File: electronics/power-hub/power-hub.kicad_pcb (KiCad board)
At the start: 2 copper layers, 120 x 70 mm, 74 parts, among them J1 24V IN, J2 ROW A, J3 ROW B, J4 ROW C, J5 ROW D, J6 ROW AUX, J7 SUPERVISOR, Q1 SUD50P06-15, U1 TPS26600PWPR, U2 TPS26600PWPR, U3 TPS26600PWPR, U4 TPS26600PWPR, U5 TPS26600PWPR

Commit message: Boards v0.2: LMR51635 buck, JST PH, drawn schematics, thermal reliefs
Addresses Fabio's review of v0.1.

Bay node (rev 0.2):
- 5 V buck: LMR51635YDDCR (60 V, 3.5 A, synchronous, 1.1 MHz) with a
  3.3 uH FXL0630, 3 x 22 uF out, 2 x 10 uF + 100 nF in, FB 120k/22k
  (5.16 V), EN 1M/100k UVLO (13.5 V on, 10.8 V off). Replaces the
  TPS54360B, its Schottky and compensation network. CIN straddles the
  VIN/GND pins on solid top-side islands with vias to In1 (TI SLUSF64B).
- 24 V in/out on JST PH (carrier notches resized, rack.yaml pwr_y).
- Power nets named along the path: 24V_BUS -> +24V -> +5V -> DUT_5V_SW
  -> shunt -> DUT_5V; the INA226 visibly runs from +3V3.
- Stackup S+GND / GND / PWR / S+GND: In2 carries +5V, +3V3 under the
  ESP32 and a protected 24 V bus strip. Outer GND pours kept (without
  them Freerouting left ~25 connections unrouted).

Power hub (rev 0.2): JST VH input instead of the screw terminal, JST PH
row outputs, eFuse limit 1.6 A (RILIM 7.5k) to protect the 2 A contacts.

Generator:
- eda.py: drawn schematic mode (sch= placement, Sheet.wire/tag/frame,
  rotated/mirrored symbols, automatic junctions, per-island labels and
  checks that no wire touches another net); all seven sheets redrawn.
- pcbgen.py: thermal reliefs on every pour (+ <board>.kicad_dru for
  single spokes on fine pitch), configurable inner layers, per-zone
  deferral, fixed vias, DRC-driven fix-up for isolated GND pads.
- JLC CPL fix for the LMR51635 (270 deg); BOM, cables, viewer, docs.

ERC 0, DRC 0 copper errors, 0 unconnected, schematic parity 0 on both.

Co-Authored-By: Claude Opus 5.5 <noreply@anthropic.com>
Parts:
- J1: footprint TerminalBlock_Phoenix:TerminalBlock_Phoenix_MKDS-1,5-2-5.08_1x02_P5.08mm_Horizontal -> Connector_JST:JST_VH_B2P-VH_1x02_P3.96mm_Vertical
- J2, J3, J4, J5, J6: footprint Connector_JST:JST_VH_B2P-VH_1x02_P3.96mm_Vertical -> Connector_JST:JST_PH_B2B-PH-K_1x02_P2.00mm_Vertical
- R21, R22, R23, R24, R25: value 5.6k -> 7.5k
- moved J2 1.00 mm to (39.0, 6.00)
- moved J3 1.00 mm to (55.0, 6.00)
- moved J4 1.00 mm to (71.0, 6.00)
- moved J5 1.00 mm to (87.0, 6.00)
- moved J6 1.00 mm to (103.0, 6.00)
- moved J1 0.60 mm to (5.60, 35.0)
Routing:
- net GND: track 546.8 -> 520.2 mm, vias 3 -> 5
- net +24V: track 385.4 -> 365.0 mm, vias 8 -> 12
- net /Outputs/ROW_AUX: track 65.8 -> 84.6 mm
- net FLT_D: track 66.2 -> 50.9 mm
- net SHDN_AUX: track 58.6 -> 43.3 mm
- net /Outputs/ROW_C: track 62.0 -> 73.2 mm
- net /Outputs/DVDT_C: track 28.3 -> 17.6 mm
- net FLT_A: track 92.6 -> 102.7 mm, vias 3 -> 2
- net /Outputs/ON_D: track 5.85 -> 15.7 mm, vias 0 -> 2
- net IMON_A: track 110.1 -> 101.2 mm
- net /Outputs/ILIM_B: track 22.7 -> 14.1 mm
- net /Outputs/ILIM_C: track 29.1 -> 21.0 mm
- net /Outputs/ROW_B: track 63.4 -> 69.9 mm
- net /Outputs/ROW_A: track 71.2 -> 77.3 mm
- net IMON_B: track 78.1 -> 83.8 mm, vias 3 -> 2
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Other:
- board text added: "hw-testing-rack · power hub v0.2"
- board text removed: "hw-testing-rack · power hub v0.1"

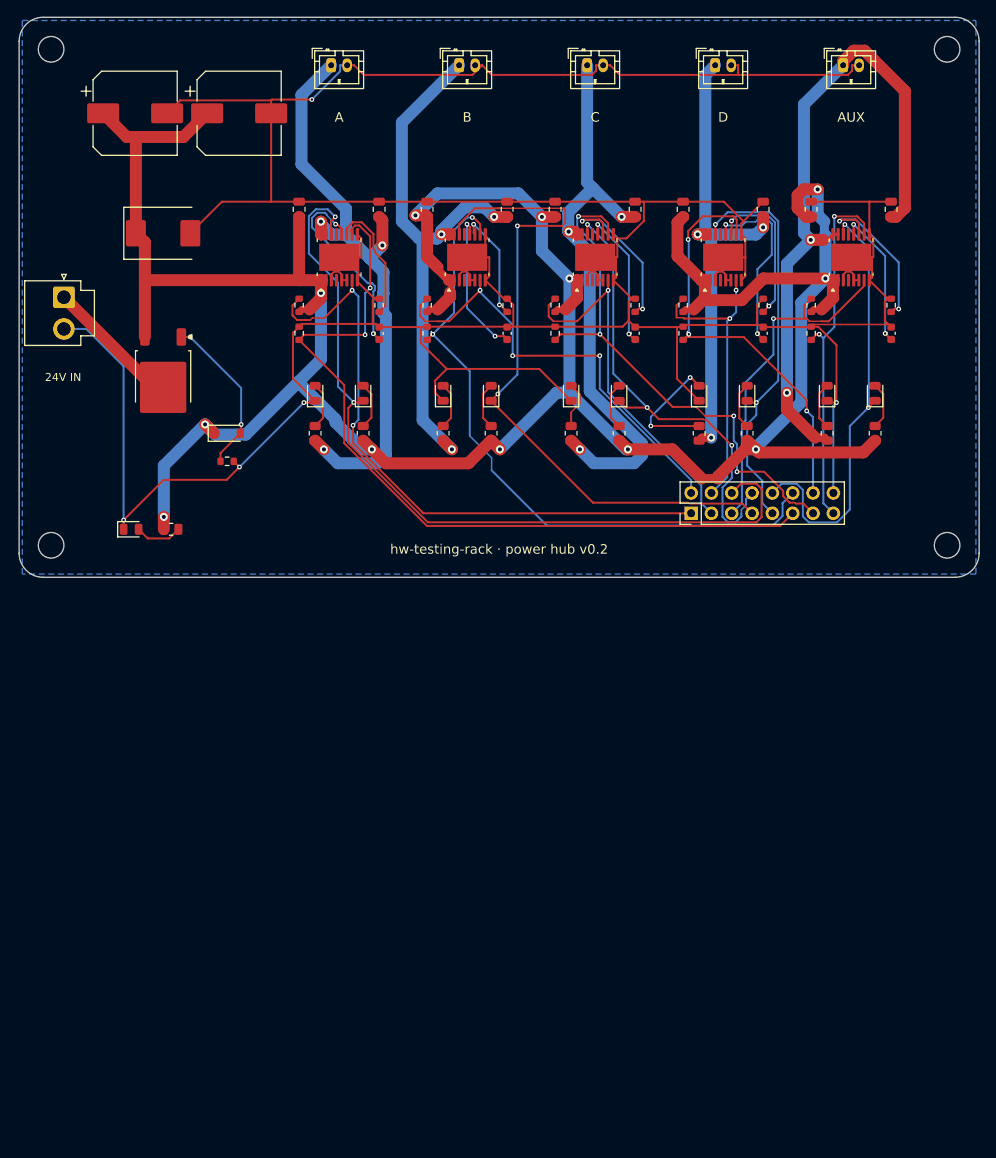
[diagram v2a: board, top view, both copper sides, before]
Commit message: Boards v0.2: Konnect review fixes (hub 24 V pours, eFuse vias, stackups)
Review of both rev 0.2 boards with the Konnect MCP server (live KiCad 10),
written up in docs/review-konnect.md.  Fixes, all through the generator:

Power hub
- 24 V path as copper pours instead of 1.5 mm tracks (up to 7.3-8 A):
  VIN_RAW from J1 to Q1's tab, +24V over Q1/D2/C1/C2, a B.Cu strip under
  the eFuse row and an IN-pin island per eFuse, joined by vias.
- six tented GND vias in each TPS26600 exposed pad, outside its mask
  opening; eFuse input/output caps moved next to their pins.
- +24V out of the Power netclass (its tracks now only feed pull-ups/LEDs).

Bay node
- AMS1117 tab: solid +3V3 island with vias to an In2 +3V3 area.
- In2 GND fill under the power pours (removed +5V islands left In2 bare).
- "PC"/"AUX" silkscreen moved off pads; DRC rule for the parts that
  overhang the outline on purpose: 0 DRC warnings (was 28).

Generator (pcbgen.py)
- stackup + finish written into the board (JLC04161H-7628 ENIG, 2-layer
  1.6 mm lead-free HASL); edge_parts DRU rule; "exclusive" pours get a
  tracks-only keep-out over their core (Freerouting routes through copper
  zones otherwise); hand-soldered pads always get thermal reliefs; GND
  "fill" zones don't count as GND layers for stitching.

ERC 0/0, DRC 0 errors / 0 warnings, 0 unconnected, parity 0 on both
boards; JLC DFM audit 0 findings.  Open: High-Speed USB in classic mode
(hand routing) and a Kelvin shunt footprint for the INA226.

Co-Authored-By: Claude Opus 5.5 <noreply@anthropic.com>
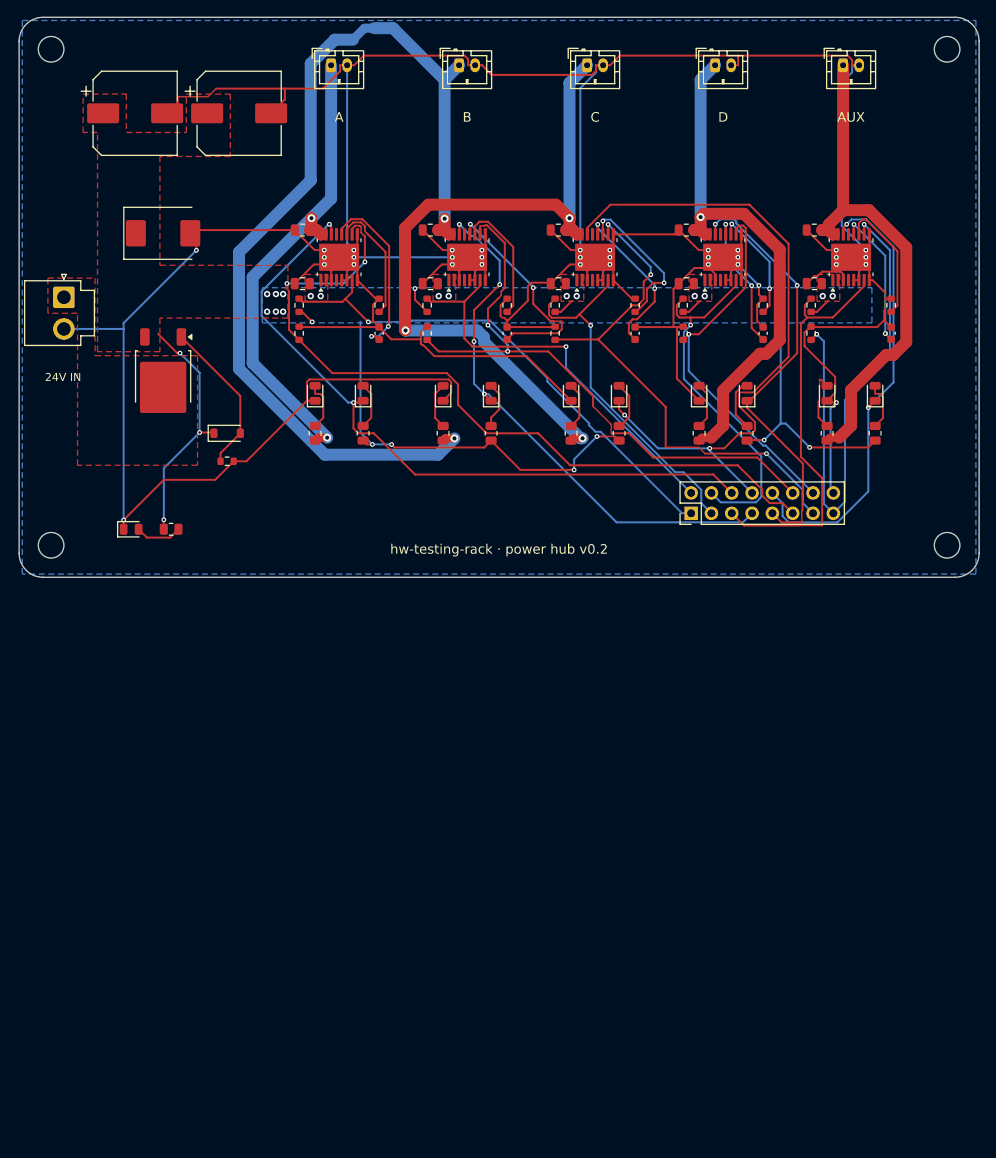
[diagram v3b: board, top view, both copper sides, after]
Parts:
- moved C31 9.95 mm to (35.4, 26.6), turned to 180 degrees
- moved C32 9.95 mm to (51.4, 26.6), turned to 180 degrees
- moved C33 9.95 mm to (67.4, 26.6), turned to 180 degrees
- moved C34 9.95 mm to (83.4, 26.6), turned to 180 degrees
- moved C35 9.95 mm to (99.4, 26.6), turned to 180 degrees
- moved C11 9.31 mm to (35.4, 33.3), turned to 180 degrees
- moved C12 9.31 mm to (51.4, 33.3), turned to 180 degrees
- moved C13 9.31 mm to (67.4, 33.3), turned to 180 degrees
- moved C14 9.31 mm to (83.4, 33.3), turned to 180 degrees
- moved C15 9.31 mm to (99.4, 33.3), turned to 180 degrees
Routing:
- net +24V: track 365.0 -> 128.4 mm, vias 12 -> 27
- net GND: track 520.2 -> 586.1 mm, vias 5 -> 34
- net /Outputs/ROW_B: track 69.9 -> 120.5 mm, vias 3 -> 2
- net FLT_C: track 59.5 -> 85.6 mm, vias 3 -> 2
- net /Outputs/ROW_AUX: track 84.6 -> 62.8 mm, vias 2 -> 0
- net IMON_AUX: track 45.7 -> 65.9 mm
- net /Outputs/ROW_A: track 77.3 -> 59.9 mm, vias 3 -> 2
- net /Input/VIN_RAW: track 17.1 -> 0.00 mm
- net FLT_B: track 84.9 -> 68.5 mm, vias 2 -> 4
- net /Outputs/ROW_C: track 73.2 -> 88.7 mm
- net FLT_A: track 102.7 -> 87.5 mm
- net SHDN_A: track 78.5 -> 63.6 mm, vias 2 -> 1
- net /Outputs/ON_D: track 15.7 -> 5.84 mm, vias 2 -> 0
- net /Outputs/DVDT_B: track 18.6 -> 27.3 mm
- net SHDN_D: track 37.3 -> 46.0 mm, vias 2 -> 1
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- added copper zone on B.Cu, net +24V
- added copper zone on F.Cu, net +24V
- added copper zone on F.Cu, net /Input/VIN_RAW

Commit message: Boards v0.3
Both boards move to revision 0.3 after the Konnect review (title blocks,
silkscreen, docs): the hub's 24 V pours and eFuse thermal vias, the stackups,
the bay node's LDO copper, Kelvin shunt and hand-routed USB High-Speed path
(see docs/review-konnect.md).  No new part type; re-quote before ordering.

Re-routed: the bay node now also fixes a via on each of J4's VBUS pads and on
U10's GND pin, the two spots Freerouting left unrouted on some runs.

ERC 0/0, DRC 0 errors / 0 warnings, 0 unconnected, parity 0 on both boards;
JLC DFM audit 0 findings.

Co-Authored-By: Claude Opus 5.5 <noreply@anthropic.com>
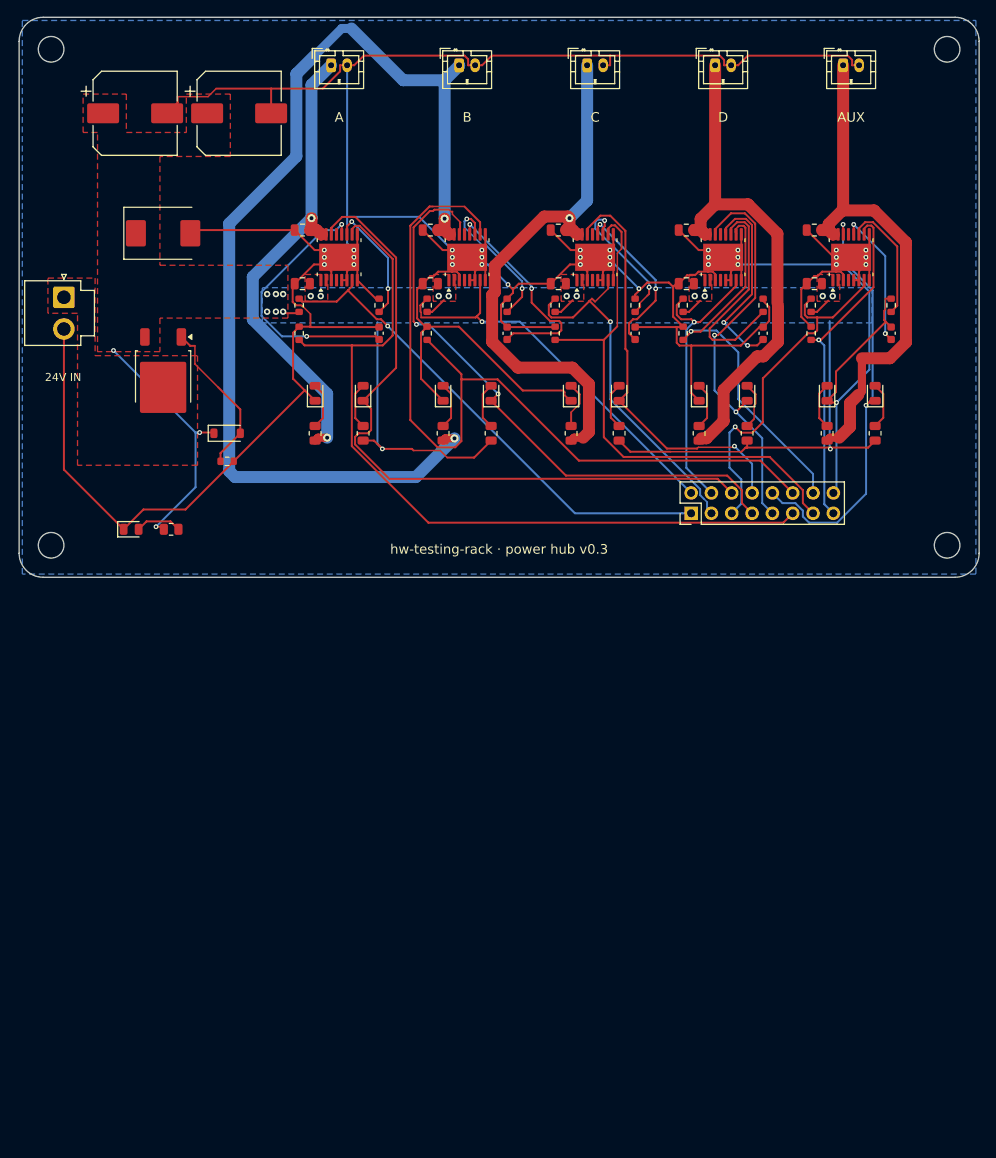
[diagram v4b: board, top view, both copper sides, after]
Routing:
- net GND: track 586.1 -> 551.6 mm, vias 34 -> 33
- net FLT_C: track 85.6 -> 52.5 mm, vias 2 -> 1
- net IMON_B: track 75.5 -> 106.2 mm, vias 2 -> 0
- net IMON_AUX: track 65.9 -> 42.6 mm, vias 2 -> 1
- net /Outputs/ROW_C: track 88.7 -> 68.3 mm, vias 3 -> 1
- net /Outputs/ILIM_D: track 14.6 -> 27.6 mm, vias 2 -> 0
- net /Outputs/ROW_B: track 120.5 -> 132.3 mm
- net /Outputs/DVDT_A: track 22.3 -> 33.7 mm
- net SHDN_D: track 46.0 -> 35.8 mm
- net /Outputs/DVDT_D: track 17.6 -> 25.0 mm
- net FLT_B: track 68.5 -> 75.9 mm, vias 4 -> 2
- net SHDN_AUX: track 51.7 -> 45.1 mm, vias 0 -> 1
- net FLT_AUX: track 58.1 -> 53.3 mm
- net FLT_D: track 54.9 -> 50.5 mm
- net IMON_A: track 97.9 -> 101.8 mm, vias 2 -> 0
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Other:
- board text added: "hw-testing-rack · power hub v0.3"
- board text removed: "hw-testing-rack · power hub v0.2"
